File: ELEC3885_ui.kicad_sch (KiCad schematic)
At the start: 60 parts, among them SW10 SW_Push, SW11 SW_Push, SW12 SW_Push, SW5 SW_Push, SW6 SW_Push, SW7 SW_Push, SW8 SW_Push, SW9 SW_Push, U4 74HC595, U5 74HC595, U6 74HC595, U7 LCD_Conn

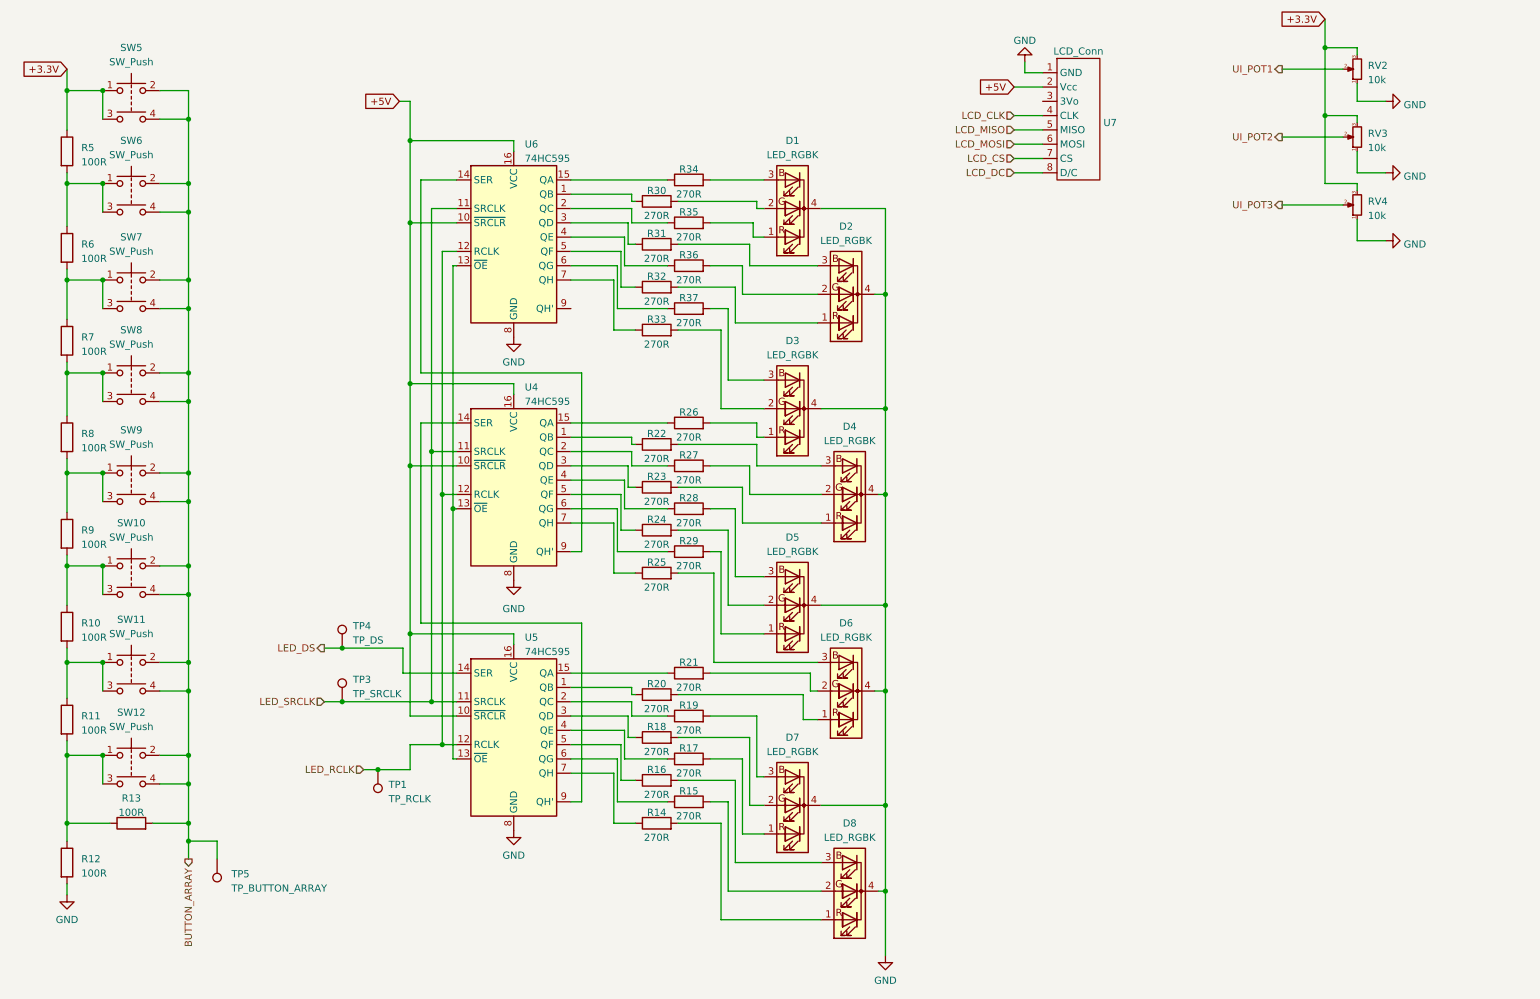
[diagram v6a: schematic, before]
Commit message: Encoders, RGB LED added, PCB cleanup
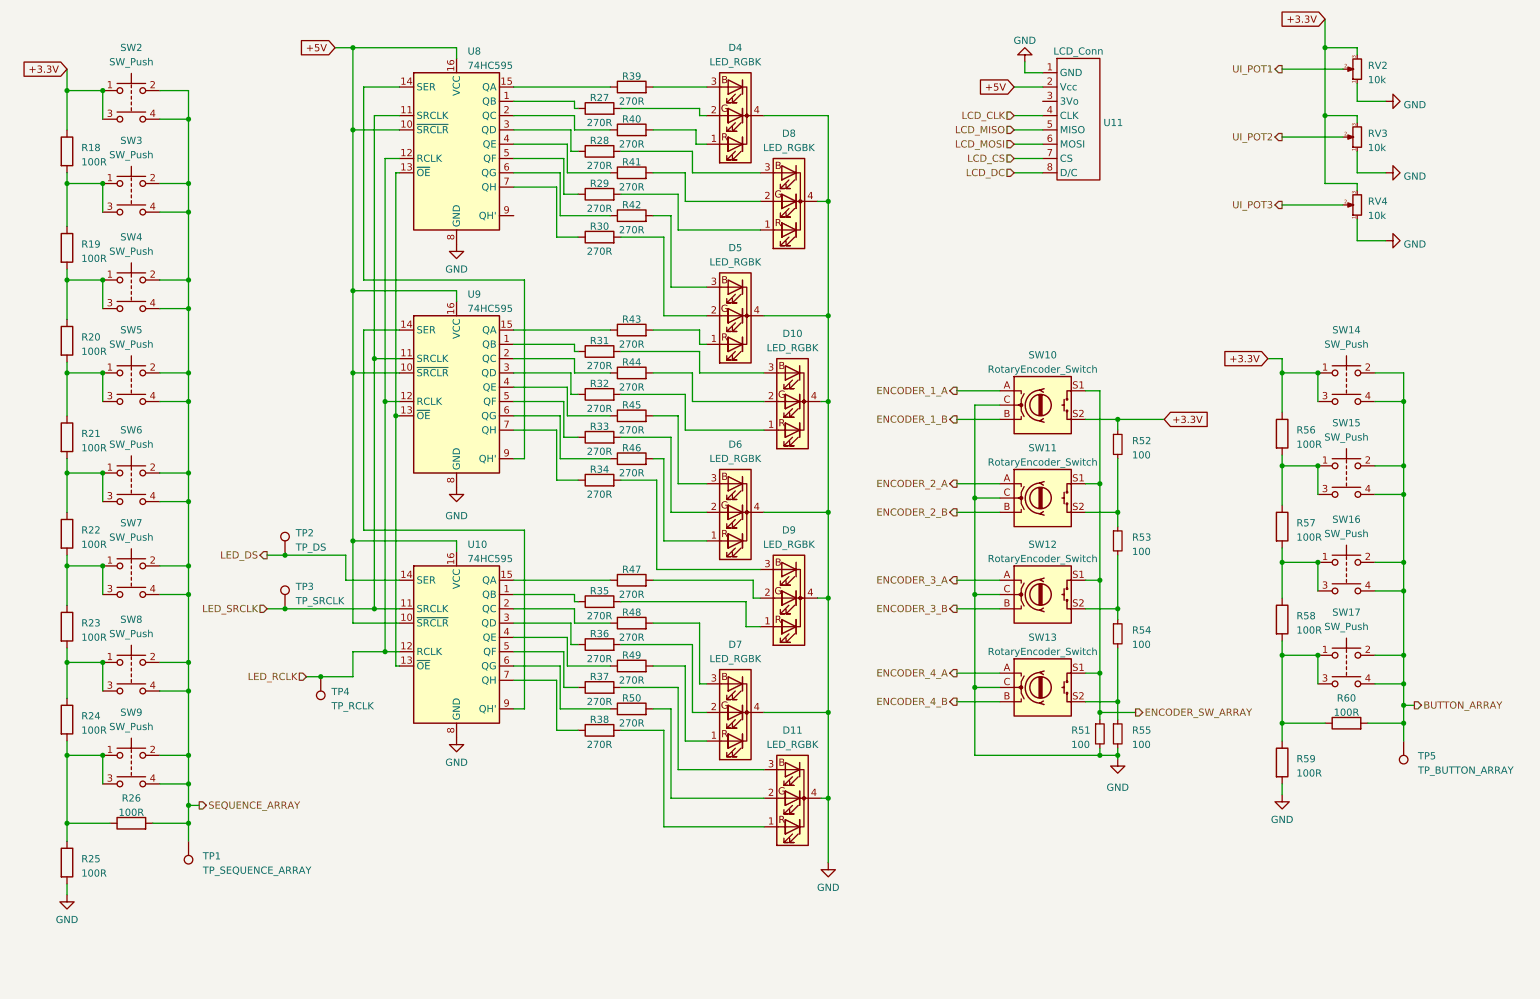
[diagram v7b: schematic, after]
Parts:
- added R51, R52, R53, R54, R55: 100, Resistor_SMD:R_0402_1005Metric, symbol Device:R_Small
- added R56, R57, R58, R59, R60: 100R, Resistor_SMD:R_0402_1005Metric, symbol Device:R
- added SW10, SW11, SW12, SW13: RotaryEncoder_Switch, Rotary_Encoder:RotaryEncoder_Alps_EC11E-Switch_Vertical_H20mm, symbol Device:RotaryEncoder_Switch
- added SW14, SW15, SW16, SW17: SW_Push, Button_Switch_SMD:SW_Push_1P1T_NO_6x6mm_H9.5mm, symbol Switch:SW_Push_Dual
- added TP5: TP_BUTTON_ARRAY, TestPoint:TestPoint_Pad_D1.0mm, symbol Connector:TestPoint
- TP1: renamed from TP5; value TP_BUTTON_ARRAY -> TP_SEQUENCE_ARRAY
- renumbered D4 to D10, D8 to D11, D1 to D4, D3 to D5, D5 to D6, D2 to D8, D6 to D9, R5 to R18, R6 to R19, R7 to R20, R8 to R21, R9 to R22, R10 to R23, R11 to R24, R12 to R25, R13 to R26, R30 to R27, R31 to R28, R32 to R29, R33 to R30, R22 to R31, R23 to R32, R24 to R33, R25 to R34, R20 to R35, R18 to R36, R16 to R37, R14 to R38, R34 to R39, R35 to R40, R36 to R41, R37 to R42, R26 to R43, R27 to R44, R28 to R45, R29 to R46, R21 to R47, R19 to R48, R17 to R49, R15 to R50, SW5 to SW2, SW6 to SW3, SW7 to SW4, SW8 to SW5, SW9 to SW6, SW10 to SW7, SW11 to SW8, SW12 to SW9, TP4 to TP2, TP1 to TP4, U5 to U10, U7 to U11, U6 to U8, U4 to U9
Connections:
- net +3.3V: now also R52.1, R56.1, SW10.S2, SW14.1, SW14.3
- net BUTTON_ARRAY: now also R60.2, SW14.2, SW14.4, SW15.2, SW15.4, SW16.2, SW16.4, SW17.2, SW17.4, TP5.1; no longer R26.2, SW2.2, SW2.4, SW3.2, SW3.4, SW4.2, SW4.4, SW5.2, SW5.4, SW6.2, SW6.4, SW7.2, SW7.4, SW8.2, SW8.4, SW9.2, SW9.4, TP1.1
- net GND: now also R51.2, R55.2, R59.2, SW10.C, SW11.C, SW12.C, SW13.C
- new net: R57.2, R58.1, SW16.1, SW16.3
- new net: R58.2, R59.1, R60.1, SW17.1, SW17.3
- new net: R54.2, R55.1, SW13.S2
- new net: R53.2, R54.1, SW12.S2
- new net: R52.2, R53.1, SW11.S2
- new net: R56.2, R57.1, SW15.1, SW15.3
- new net ENCODER_1_A: SW10.A
- new net ENCODER_1_B: SW10.B
- new net ENCODER_2_A: SW11.A
- new net ENCODER_2_B: SW11.B
- new net ENCODER_3_A: SW12.A
- new net ENCODER_3_B: SW12.B
- new net ENCODER_4_A: SW13.A
- new net ENCODER_4_B: SW13.B
- new net ENCODER_SW_ARRAY: R51.1, SW10.S1, SW11.S1, SW12.S1, SW13.S1
- new net SEQUENCE_ARRAY: R26.2, SW2.2, SW2.4, SW3.2, SW3.4, SW4.2, SW4.4, SW5.2, SW5.4, SW6.2, SW6.4, SW7.2, SW7.4, SW8.2, SW8.4, SW9.2, SW9.4, TP1.1
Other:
- moved on the sheet: D10, D11, D4, D5, D6, D7, D8, D9, R27, R28, R29, R30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

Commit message: Testpoints added, silkscreen cleaned
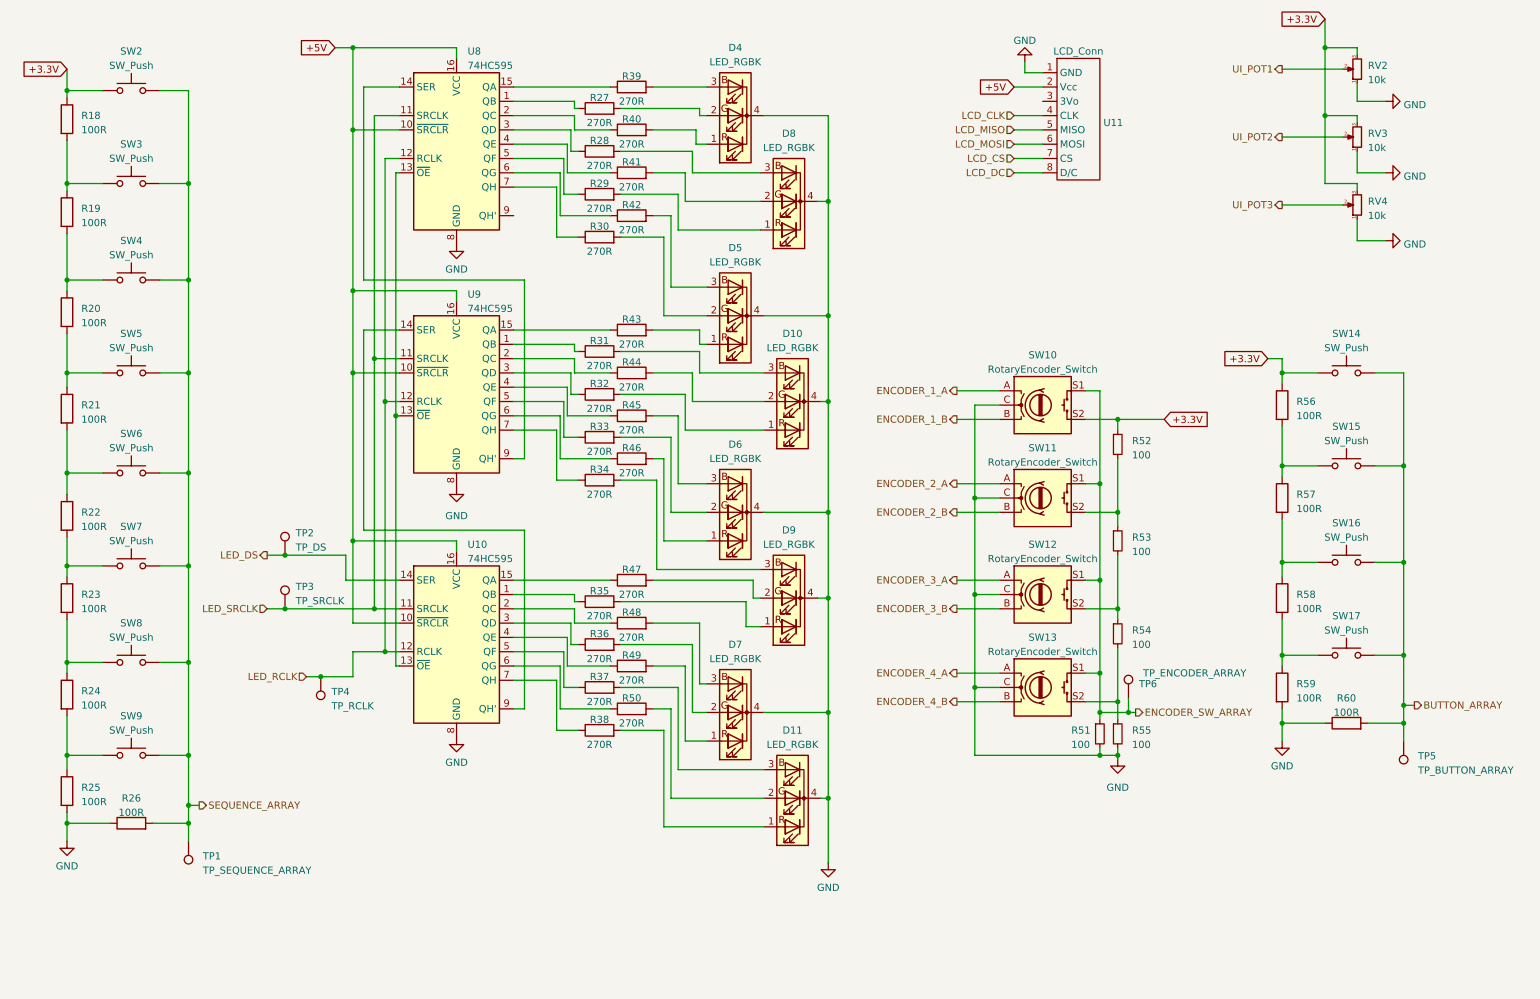
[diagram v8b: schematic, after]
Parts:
- removed SW14, SW15, SW16, SW17, SW2, SW3, SW4, SW5, SW6, SW7, SW8, SW9: SW_Push, Button_Switch_SMD:SW_Push_1P1T_NO_6x6mm_H9.5mm, symbol Switch:SW_Push_Dual
- added SW14, SW15, SW16, SW17, SW2, SW3, SW4, SW5, SW6, SW7, SW8, SW9: SW_Push, Button_Switch_Keyboard:SW_Cherry_MX_1.00u_PCB, symbol Switch:SW_Push
- added TP6: TP_ENCODER_ARRAY, TestPoint:TestPoint_Pad_D1.0mm, symbol Connector:TestPoint
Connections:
- net +3.3V: now also SW14.1, SW2.1
- net BUTTON_ARRAY: now also SW14.2, SW15.2, SW16.2, SW17.2
- net ENCODER_SW_ARRAY: now also TP6.1
- net GND: now also R26.1, R60.1
- net SEQUENCE_ARRAY: now also SW2.2, SW3.2, SW4.2, SW5.2, SW6.2, SW7.2, SW8.2, SW9.2
- net at R24.2, R25.1: now also SW9.1; no longer R26.1
- net at R23.2, R24.1: now also SW8.1
- net at R18.2, R19.1: now also SW3.1
- net at R19.2, R20.1: now also SW4.1
- net at R22.2, R23.1: now also SW7.1
- net at R20.2, R21.1: now also SW5.1
- net at R57.2, R58.1: now also SW16.1
- net at R58.2, R59.1: now also SW17.1; no longer R60.1
- net at R21.2, R22.1: now also SW6.1
- net at R56.2, R57.1: now also SW15.1
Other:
- moved on the sheet: R18, R19, R20, R21, R22, R23, R24, R25, R56, R57, R58, R59
